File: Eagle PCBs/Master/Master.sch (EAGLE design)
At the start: 15 parts

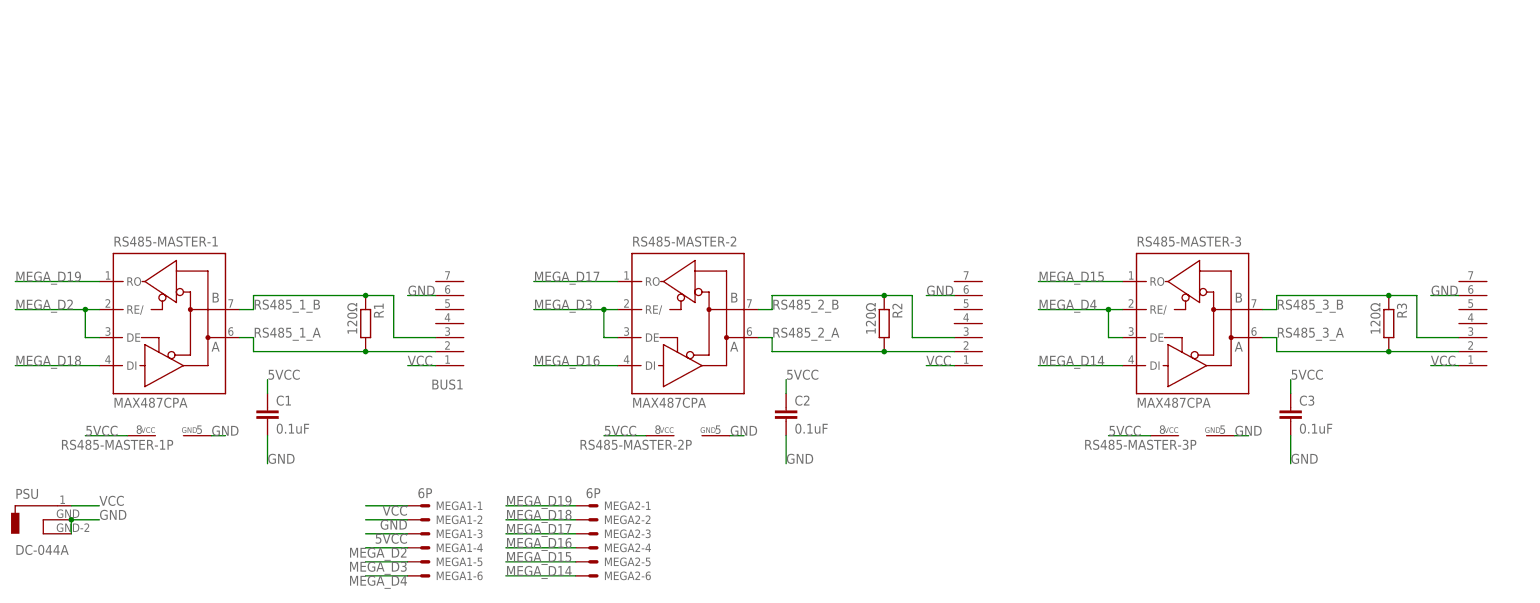
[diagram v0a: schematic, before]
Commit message: Minor PCB adjustments
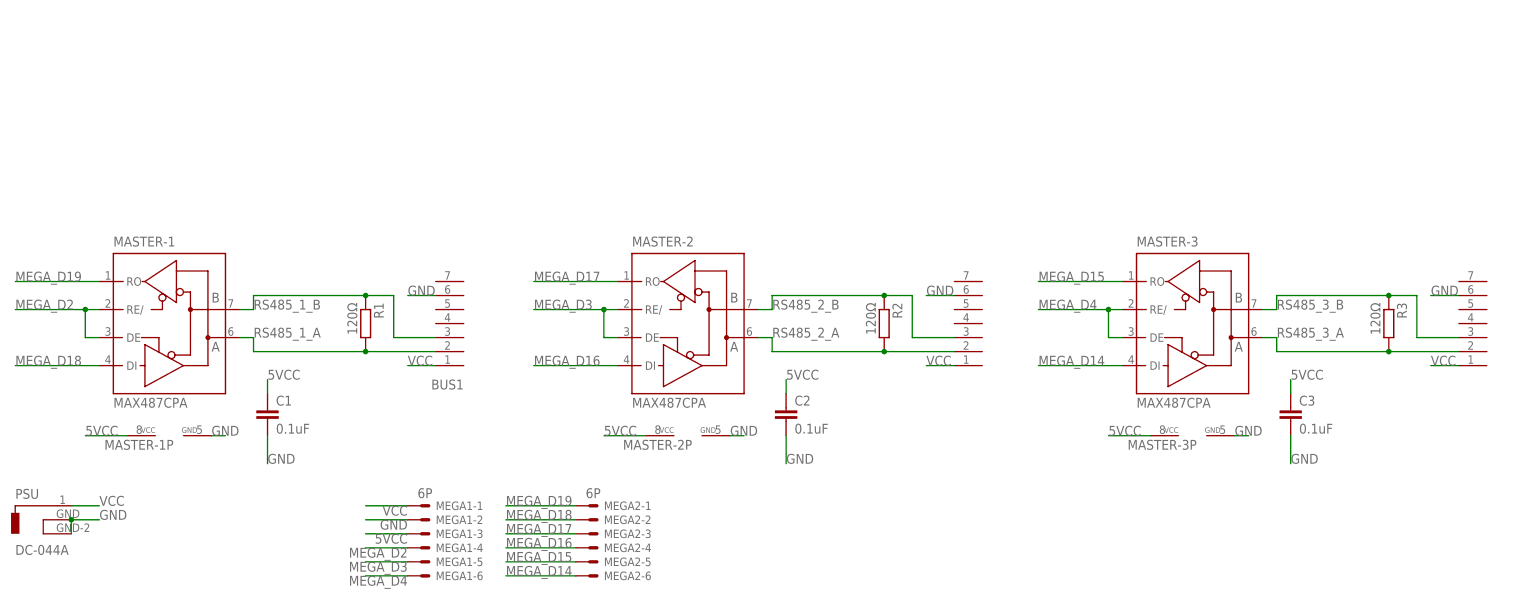
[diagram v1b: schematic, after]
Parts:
- renumbered RS485-MASTER-1 to MASTER-1, RS485-MASTER-2 to MASTER-2, RS485-MASTER-3 to MASTER-3

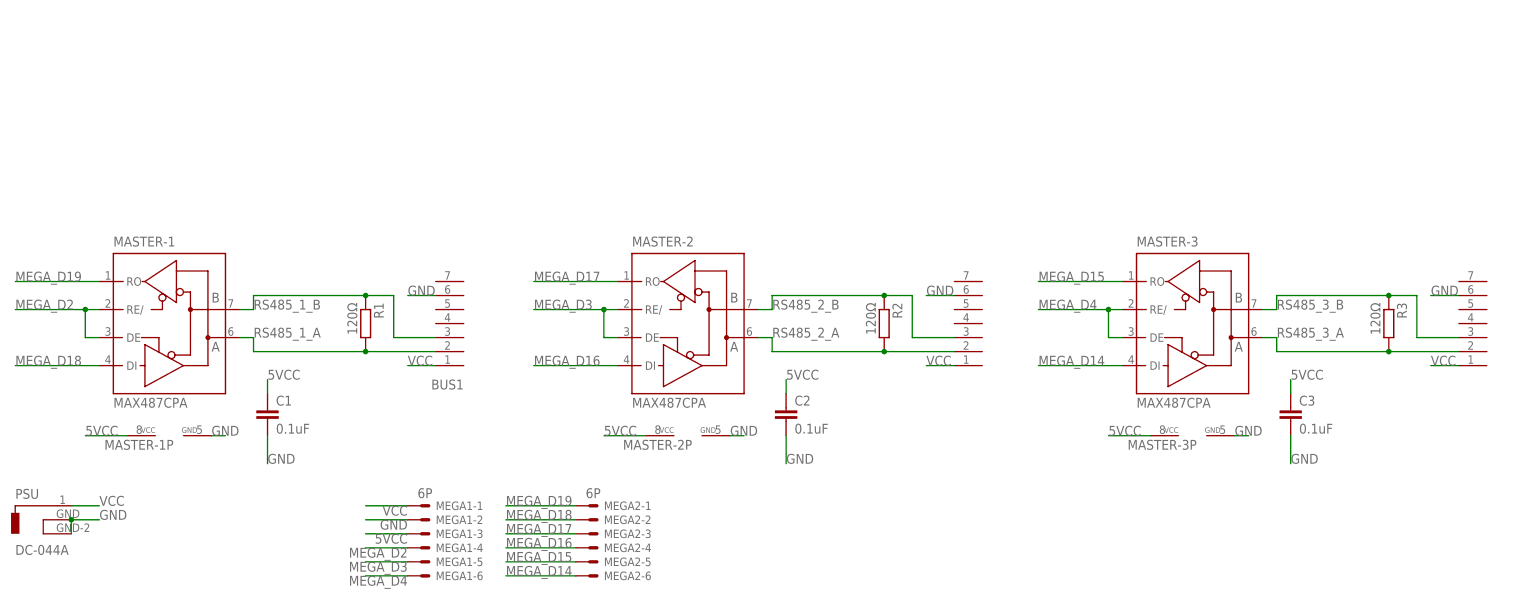
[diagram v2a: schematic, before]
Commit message: Added a 5v bus to all PCBs
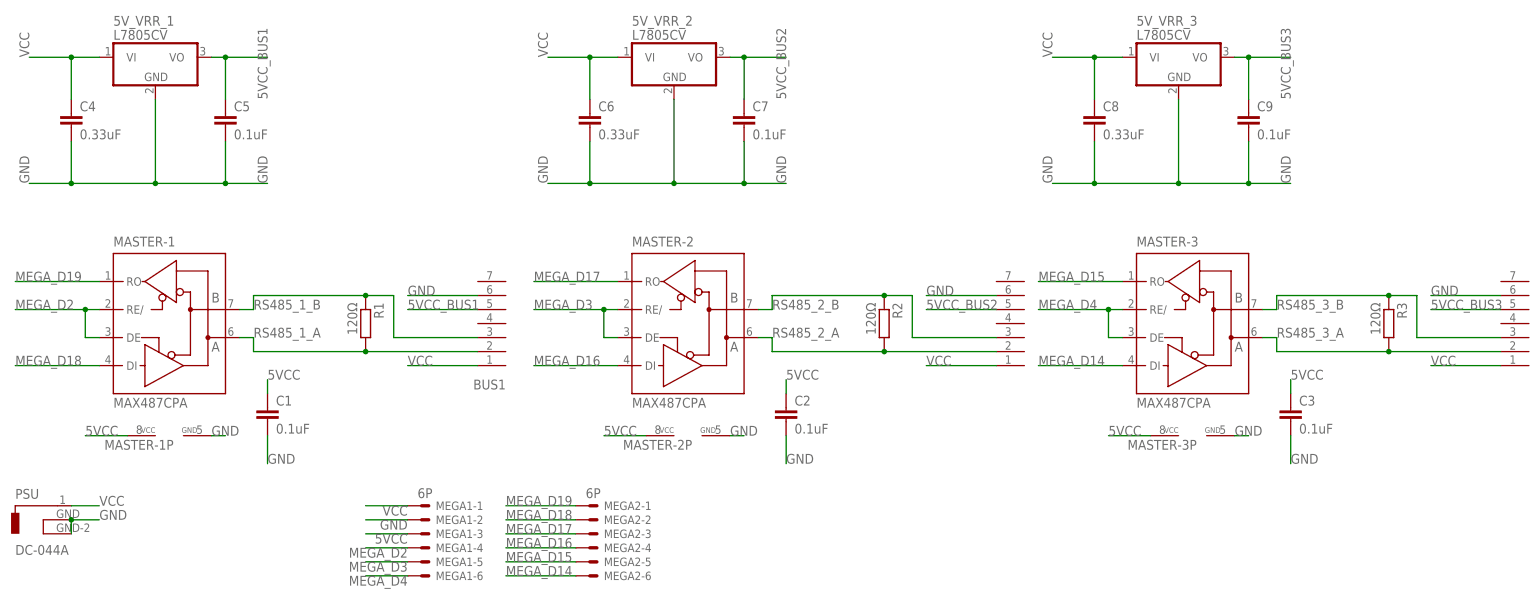
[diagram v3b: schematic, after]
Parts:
- added 5V_VRR_1, 5V_VRR_2, 5V_VRR_3: L7805CV, linear:7805T
- added C4, C6, C8: 0.33uF, rcl:C-EU025-025X050
- added C5, C7, C9: 0.1uF, rcl:C-EU025-025X050
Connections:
- new net 5VCC_BUS1: 5V_VRR_1.VO, BUS1.5, C5.1
- new net 5VCC_BUS2: 5V_VRR_2.VO, BUS2.5, C7.1
- new net 5VCC_BUS3: 5V_VRR_3.VO, BUS3.5, C9.1
- net GND: now also 5V_VRR_1.GND, 5V_VRR_2.GND, 5V_VRR_3.GND, C4.2, C5.2, C6.2, C7.2, C8.2, C9.2
- net VCC: now also 5V_VRR_1.VI, 5V_VRR_2.VI, 5V_VRR_3.VI, C4.1, C6.1, C8.1
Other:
- moved on the sheet: BUS1
